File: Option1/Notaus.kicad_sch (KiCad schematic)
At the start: 3 parts, among them Q901 AON6284

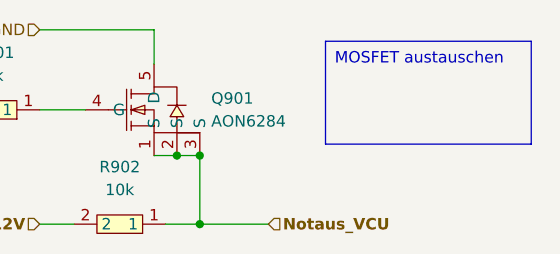
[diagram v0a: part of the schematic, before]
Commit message: SPI Flash hinzugefügt, IN/Outputs vereinheitlicht, USB Flash Möglichkeit hinzugefügt, Display fehtl noch
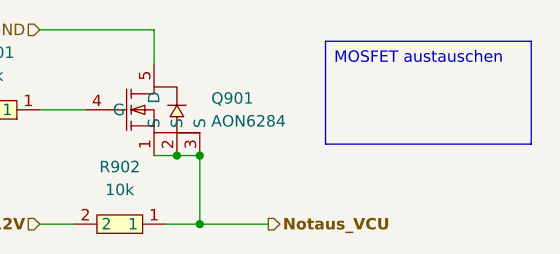
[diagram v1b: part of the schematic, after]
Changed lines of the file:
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@@
 (kicad_sch
-	(version 20231120)
+	(version 20250114)
 	(generator "eeschema")
-	(generator_version "8.0")
+	(generator_version "9.0")
 	(paper "A4")
 	(title_block
@@
 		(comment 2 "Bachelorarbiet")
 		(comment 3 "Sebastian Hampl")
+	)
+	(text_box "MOSFET austauschen"
+		(exclude_from_sim no)
+		(at 132.08 64.77 0)
+		(size 22.86 11.43)
+		(margins 0.9525 0.9525 0.9525 0.9525)
+		(stroke
+			(width 0)
+			(type default)
+			(color 255 0 0 1)
+		)
+		(fill
+			(type none)
+		)
+		(effects
+			(font
+				(size 1.27 1.27)
+			)
+			(justify left top)
+		)
 	)
 	(junction
@@
 		)
 	)
-	(text_box "MOSFET austauschen"
-		(exclude_from_sim no)
-		(at 132.08 64.77 0)
-		(size 22.86 11.43)
-		(stroke
-			(width 0)
-			(type default)
-			(color 255 0 0 1)
-		)
-		(fill
-			(type none)
-		)
-		(effects
-			(font
-				(size 1.27 1.27)
-			)
-			(justify left top)
-		)
-	)
 	(hierarchical_label "Notaus_VCU"
-		(shape input)
+		(shape output)
 		(at 125.73 85.09 0)
 		(effects

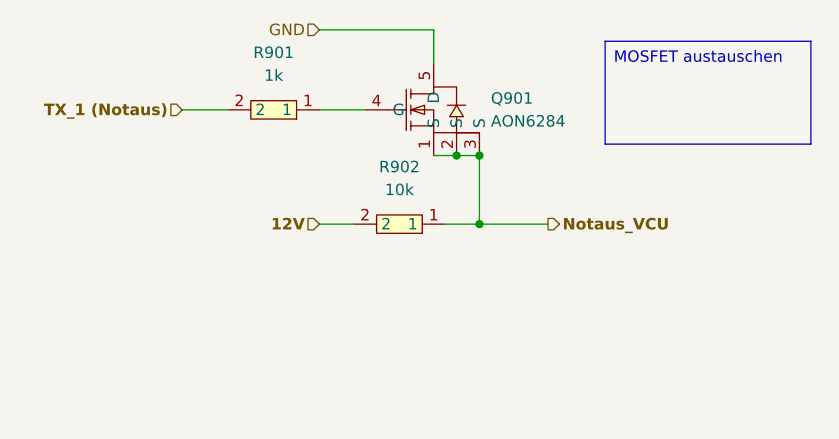
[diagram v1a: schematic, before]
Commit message: USB auf 3V3 umgebaut
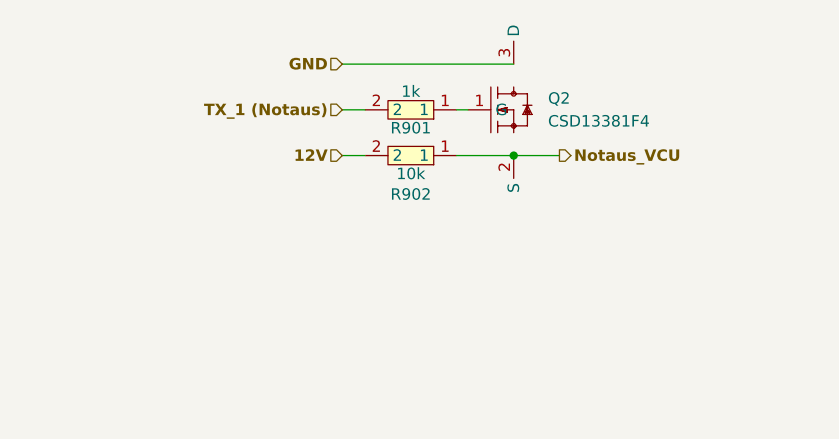
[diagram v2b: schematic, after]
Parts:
- removed Q901: AON6284, easyeda2kicad:POWERVDFN-8_L6.2-W5.2-P1.27-LS6.0-BL, symbol easyeda2kicad:AON6284
- added Q2: CSD13381F4, easyeda2kicad:PICOSTAR-3_L1.0-W0.6-P0.40-S0.65-BL-1, symbol EasyEda2KiCad:CSD13381F4
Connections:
- net GND: now also Q2.3 (D)
- net Notaus_VCU: now also Q2.2 (S)
- net at R901.1: now also Q2.1 (G)
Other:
- moved on the sheet: R901, R902

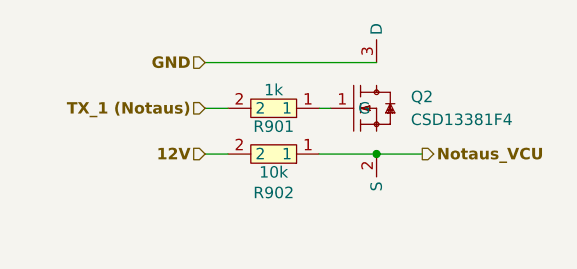
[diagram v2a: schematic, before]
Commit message: Transitor getauscht, Pulldown Widerstände für Definierten LOW Pegel hinzugefügt
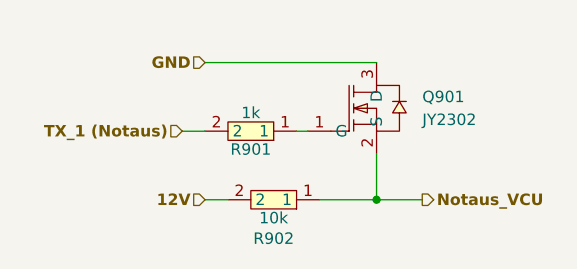
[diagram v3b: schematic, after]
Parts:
- removed Q2: CSD13381F4, easyeda2kicad:PICOSTAR-3_L1.0-W0.6-P0.40-S0.65-BL-1, symbol EasyEda2KiCad:CSD13381F4
- added Q901: JY2302, easyeda2kicad:SOT-23-3_L2.9-W1.3-P0.95-LS2.4-BR, symbol EasyEda2KiCad:JY2302
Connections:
- net GND: now also Q901.3 (D)
- net Notaus_VCU: now also Q901.2 (S)
- net at R901.1: now also Q901.1 (G)
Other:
- moved on the sheet: R901, R902
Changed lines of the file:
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@@
 	)
 	(junction
-		(at 121.92 77.47)
+		(at 121.92 82.55)
 		(diameter 0)
 		(color 0 0 0 0)
@@
 	(wire
 		(pts
-			(xy 121.92 77.47) (xy 127 77.47)
-		)
-		(stroke
-			(width 0)
-			(type default)
-		)
-	)
-	(wire
-		(pts
-			(xy 116.84 72.39) (xy 115.57 72.39)
-		)
-		(stroke
-			(width 0)
-			(type default)
-		)
-	)
-	(wire
-		(pts
-			(xy 102.87 72.39) (xy 105.41 72.39)
-		)
-		(stroke
-			(width 0)
-			(type default)
-		)
-	)
-	(wire
-		(pts
-			(xy 115.57 77.47) (xy 121.92 77.47)
-		)
-		(stroke
-			(width 0)
-			(type default)
-		)
-	)
-	(wire
-		(pts
-			(xy 102.87 77.47) (xy 105.41 77.47)
+			(xy 115.57 82.55) (xy 121.92 82.55)
+		)
+		(stroke
+			(width 0)
+			(type default)
+		)
+	)
+	(wire
+		(pts
+			(xy 114.3 74.93) (xy 113.03 74.93)
+		)
+		(stroke
+			(width 0)
+			(type default)
+		)
+	)
+	(wire
+		(pts
+			(xy 121.92 82.55) (xy 127 82.55)
+		)
+		(stroke
+			(width 0)
+			(type default)
+		)
+	)
+	(wire
+		(pts
+			(xy 100.33 74.93) (xy 102.87 74.93)
+		)
+		(stroke
+			(width 0)
+			(type default)
+		)
+	)
+	(wire
+		(pts
+			(xy 121.92 82.55) (xy 121.92 77.47)
+		)
+		(stroke
+			(width 0)
+			(type default)
+		)
+	)
+	(wire
+		(pts
+			(xy 102.87 82.55) (xy 105.41 82.55)
 		)
 		(stroke
@@
 	(hierarchical_label "Notaus_VCU"
 		(shape output)
-		(at 127 77.47 0)
+		(at 127 82.55 0)
 		(effects
 			(font
@@
 	(hierarchical_label "12V"
 		(shape input)
-		(at 102.87 77.47 180)
+		(at 102.87 82.55 180)
 		(effects
 			(font
@@
 	(hierarchical_label "TX_1 (Notaus)"
 		(shape input)
-		(at 102.87 72.39 180)
+		(at 100.33 74.93 180)
 		(effects
 			(font
@@
 	(symbol
 		(lib_id "easyeda2kicad:0603WAF1001T5E")
-		(at 110.49 72.39 180)
+		(at 107.95 74.93 180)
 		(unit 1)
 		(exclude_from_sim no)
@@
 		(dnp no)
 		(property "Reference" "R901"
-			(at 110.49 74.422 0)
+			(at 107.95 76.962 0)
 			(effects
 				(font
@@
 		)
 		(property "Value" "1k"
-			(at 110.49 70.358 0)
+			(at 107.95 72.898 0)
 			(effects
 				(font
@@
 		)
 		(property "Footprint" "easyeda2kicad:R0603"
-			(at 110.49 64.77 0)
+			(at 107.95 67.31 0)
 			(effects
 				(font
@@
 		)
 		(property "Datasheet" "https://lcsc.com/product-detail/Chip-Resistor-Surface-Mount-UniOhm_1KR-1001-1_C21190.html"
-			(at 110.49 62.23 0)
+			(at 107.95 64.77 0)
 			(effects
 				(font
@@
 		)
 		(property "Description" ""
-			(at 110.49 72.39 0)
+			(at 107.95 74.93 0)
 			(effects
 				(font
@@
 		)
 		(property "LCSC Part" "C21190"
-			(at 110.49 59.69 0)
+			(at 107.95 62.23 0)
 			(effects
 				(font
@@
 	)
 	(symbol
-		(lib_id "EasyEda2KiCad:CSD13381F4")
+		(lib_id "EasyEda2KiCad:JY2302")
 		(at 119.38 72.39 0)
 		(unit 1)
@@
 		(dnp no)
 		(fields_autoplaced yes)
-		(property "Reference" "Q2"
-			(at 125.73 71.1199 0)
+		(property "Reference" "Q901"
+			(at 127 71.1199 0)
 			(effects
 				(font
@@
 			)
 		)
-		(property "Value" "CSD13381F4"
-			(at 125.73 73.6599 0)
+		(property "Value" "JY2302"
+			(at 127 73.6599 0)
 			(effects
 				(font
@@
 			)
 		)
-		(property "Footprint" "easyeda2kicad:PICOSTAR-3_L1.0-W0.6-P0.40-S0.65-BL-1"
+		(property "Footprint" "easyeda2kicad:SOT-23-3_L2.9-W1.3-P0.95-LS2.4-BR"
 			(at 119.38 85.09 0)
 			(effects
@@
 			)
 		)
-		(property "LCSC Part" "C179868"
+		(property "LCSC Part" "C3038095"
 			(at 119.38 87.63 0)
 			(effects
@@
 			)
 		)
+		(pin "2"
+		)
+		(pin "1"
+		)
 		(pin "3"
 		)
-		(pin "1"
-		)
-		(pin "2"
-		)
 		(instances
-			(project "Option1"
+			(project ""
 				(path "/b9e5f262-9648-4b79-bdd1-af888b822329/75c49fff-0cff-45a7-88f1-e27f7e1370db"
-					(reference "Q2")
+					(reference "Q901")
 					(unit 1)
 				)
@@
 	(symbol
 		(lib_id "easyeda2kicad:0603WAF1002T5E")
-		(at 110.49 77.47 180)
+		(at 110.49 82.55 180)
 		(unit 1)
 		(exclude_from_sim no)
@@
 		(dnp no)
 		(property "Reference" "R902"
-			(at 110.49 81.788 0)
+			(at 110.49 86.868 0)
 			(effects
 				(font
@@
 		)
 		(property "Value" "10k"
-			(at 110.49 79.502 0)
+			(at 110.49 84.582 0)
 			(effects
 				(font
@@
 		)
 		(property "Footprint" "easyeda2kicad:R0603"
+			(at 110.49 74.93 0)
+			(effects
+				(font
+					(size 1.27 1.27)
+				)
+				(hide yes)
+			)
+		)
+		(property "Datasheet" "https://lcsc.com/product-detail/Chip-Resistor-Surface-Mount-UniOhm_10KR-1002-1_C25804.html"
+			(at 110.49 72.39 0)
+			(effects
+				(font
+					(size 1.27 1.27)
+				)
+				(hide yes)
+			)
+		)
+		(property "Description" ""
+			(at 110.49 82.55 0)
+			(effects
+				(font
+					(size 1.27 1.27)
+				)
+				(hide yes)
+			)
+		)
+		(property "LCSC Part" "C25804"
 			(at 110.49 69.85 0)
 			(effects
 				(font
-					(size 1.27 1.27)
-				)
-				(hide yes)
-			)
-		)
-		(property "Datasheet" "https://lcsc.com/product-detail/Chip-Resistor-Surface-Mount-UniOhm_10KR-1002-1_C25804.html"
-			(at 110.49 67.31 0)
-			(effects
-				(font
-					(size 1.27 1.27)
-				)
-				(hide yes)
-			)
-		)
-		(property "Description" ""
-			(at 110.49 77.47 0)
-			(effects
-				(font
-					(size 1.27 1.27)
-				)
-				(hide yes)
-			)
-		)
-		(property "LCSC Part" "C25804"
-			(at 110.49 64.77 0)
-			(effects
-				(font

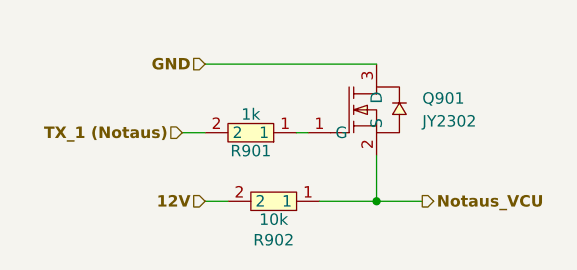
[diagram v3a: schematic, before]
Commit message: MCT und SPI zu Layout hinzugefügt
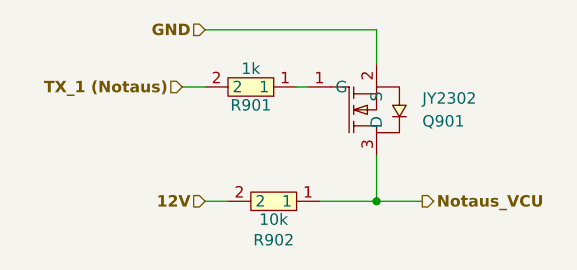
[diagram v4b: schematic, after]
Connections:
- net GND: now also Q901.2 (S); no longer Q901.3 (D)
- net Notaus_VCU: now also Q901.3 (D); no longer Q901.2 (S)
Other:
- moved on the sheet: R901
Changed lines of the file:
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@@
 	(wire
 		(pts
-			(xy 102.87 67.31) (xy 121.92 67.31)
+			(xy 102.87 63.5) (xy 121.92 63.5)
 		)
 		(stroke
@@
 	(wire
 		(pts
-			(xy 114.3 74.93) (xy 113.03 74.93)
+			(xy 100.33 69.85) (xy 102.87 69.85)
+		)
+		(stroke
+			(width 0)
+			(type default)
+		)
+	)
+	(wire
+		(pts
+			(xy 114.3 69.85) (xy 113.03 69.85)
 		)
 		(stroke
@@
 	(wire
 		(pts
-			(xy 100.33 74.93) (xy 102.87 74.93)
+			(xy 121.92 63.5) (xy 121.92 67.31)
 		)
 		(stroke
@@
 	(hierarchical_label "TX_1 (Notaus)"
 		(shape input)
-		(at 100.33 74.93 180)
+		(at 100.33 69.85 180)
 		(effects
 			(font
@@
 	(hierarchical_label "GND"
 		(shape input)
-		(at 102.87 67.31 180)
+		(at 102.87 63.5 180)
 		(effects
 			(font
@@
 	(symbol
 		(lib_id "easyeda2kicad:0603WAF1001T5E")
-		(at 107.95 74.93 180)
+		(at 107.95 69.85 180)
 		(unit 1)
 		(exclude_from_sim no)
@@
 		(dnp no)
 		(property "Reference" "R901"
-			(at 107.95 76.962 0)
+			(at 107.95 71.882 0)
 			(effects
 				(font
@@
 		)
 		(property "Value" "1k"
-			(at 107.95 72.898 0)
+			(at 107.95 67.818 0)
 			(effects
 				(font
@@
 		)
 		(property "Footprint" "easyeda2kicad:R0603"
-			(at 107.95 67.31 0)
+			(at 107.95 62.23 0)
 			(effects
 				(font
@@
 		)
 		(property "Datasheet" "https://lcsc.com/product-detail/Chip-Resistor-Surface-Mount-UniOhm_1KR-1001-1_C21190.html"
-			(at 107.95 64.77 0)
+			(at 107.95 59.69 0)
 			(effects
 				(font
@@
 		)
 		(property "Description" ""
-			(at 107.95 74.93 0)
+			(at 107.95 69.85 0)
 			(effects
 				(font
@@
 		)
 		(property "LCSC Part" "C21190"
-			(at 107.95 62.23 0)
+			(at 107.95 57.15 0)
 			(effects
 				(font
@@
 		(lib_id "EasyEda2KiCad:JY2302")
 		(at 119.38 72.39 0)
+		(mirror x)
 		(unit 1)
 		(exclude_from_sim no)
@@
 		(on_board yes)
 		(dnp no)
-		(fields_autoplaced yes)
 		(property "Reference" "Q901"
-			(at 127 71.1199 0)
+			(at 127 73.6601 0)
 			(effects
 				(font
@@
 		)
 		(property "Value" "JY2302"
-			(at 127 73.6599 0)
+			(at 127 71.1201 0)
 			(effects
 				(font
@@
 		)
 		(property "Footprint" "easyeda2kicad:SOT-23-3_L2.9-W1.3-P0.95-LS2.4-BR"
-			(at 119.38 85.09 0)
+			(at 119.38 59.69 0)
 			(effects
 				(font
@@
 		)
 		(property "LCSC Part" "C3038095"
-			(at 119.38 87.63 0)
-			(effects
-				(font
+			(at 119.38 57.15 0)
+			(effects
+				(font

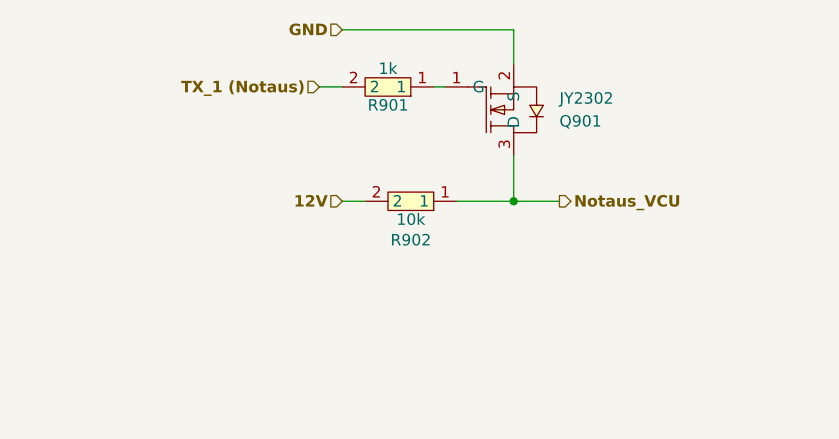
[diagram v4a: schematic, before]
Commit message: LEDs an Transistoren hinzugefügt, Layout angepasst, LEDs eingefügt, LEDs zeigen an, ob Transsitor durchgeschalten ist
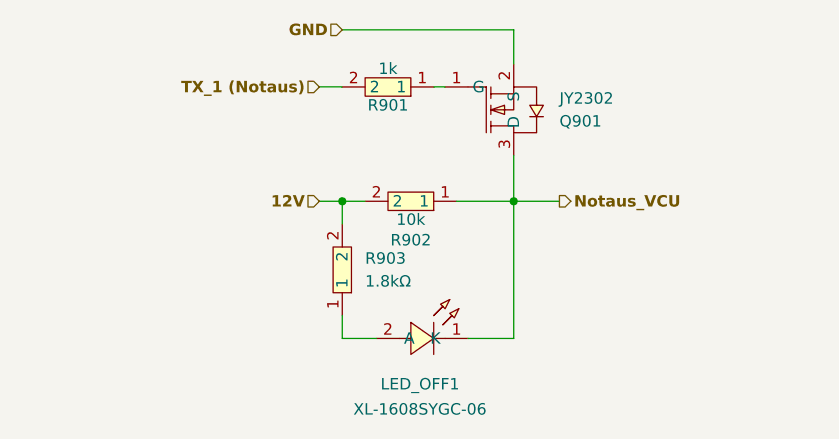
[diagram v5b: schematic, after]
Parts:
- added LED_OFF1: XL-1608SYGC-06, easyeda2kicad:LED0603-RD_GREEN, symbol EasyEda2KiCad:XL-1608SYGC-06
- added R903: 1.8kΩ, easyeda2kicad:R0603, symbol EasyEda2KiCad:0603WAF1801T5E
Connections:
- net 12V: now also R903.2
- net Notaus_VCU: now also LED_OFF1.1 (K)
- new net: LED_OFF1.2 (A), R903.1
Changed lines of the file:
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@@
 		(color 0 0 0 0)
 	)
+	(junction
+		(at 102.87 82.55)
+		(diameter 0)
+		(color 0 0 0 0)
+	)
+	(wire
+		(pts
+			(xy 102.87 82.55) (xy 102.87 85.09)
+		)
+		(stroke
+			(width 0)
+			(type default)
+		)
+	)
+	(wire
+		(pts
+			(xy 102.87 82.55) (xy 105.41 82.55)
+		)
+		(stroke
+			(width 0)
+			(type default)
+		)
+	)
+	(wire
+		(pts
+			(xy 116.84 97.79) (xy 121.92 97.79)
+		)
+		(stroke
+			(width 0)
+			(type default)
+		)
+	)
 	(wire
 		(pts
@@
 	(wire
 		(pts
+			(xy 106.68 97.79) (xy 102.87 97.79)
+		)
+		(stroke
+			(width 0)
+			(type default)
+		)
+	)
+	(wire
+		(pts
+			(xy 121.92 97.79) (xy 121.92 82.55)
+		)
+		(stroke
+			(width 0)
+			(type default)
+		)
+	)
+	(wire
+		(pts
 			(xy 121.92 63.5) (xy 121.92 67.31)
 		)
@@
 	(wire
 		(pts
+			(xy 102.87 97.79) (xy 102.87 95.25)
+		)
+		(stroke
+			(width 0)
+			(type default)
+		)
+	)
+	(wire
+		(pts
 			(xy 121.92 82.55) (xy 121.92 77.47)
 		)
@@
 	(wire
 		(pts
-			(xy 102.87 82.55) (xy 105.41 82.55)
+			(xy 100.33 82.55) (xy 102.87 82.55)
 		)
 		(stroke
@@
 	(hierarchical_label "12V"
 		(shape input)
-		(at 102.87 82.55 180)
+		(at 100.33 82.55 180)
 		(effects
 			(font
@@
 					(unit 1)
 				)
+			)
+		)
+	)
+	(symbol
+		(lib_id "EasyEda2KiCad:XL-1608SYGC-06")
+		(at 111.76 97.79 0)
+		(mirror y)
+		(unit 1)
+		(exclude_from_sim no)
+		(in_bom yes)
+		(on_board yes)
+		(dnp no)
+		(property "Reference" "LED_OFF1"
+			(at 111.506 102.87 0)
+			(effects
+				(font
+					(size 1.27 1.27)
+				)
+			)
+		)
+		(property "Value" "XL-1608SYGC-06"
+			(at 111.506 105.664 0)
+			(effects
+				(font
+					(size 1.27 1.27)
+				)
+			)
+		)
+		(property "Footprint" "easyeda2kicad:LED0603-RD_GREEN"
+			(at 111.76 105.41 0)
+			(effects
+				(font
+					(size 1.27 1.27)
+				)
+				(hide yes)
+			)
+		)
+		(property "Datasheet" ""
+			(at 111.76 97.79 0)
+			(effects
+				(font
+					(size 1.27 1.27)
+				)
+				(hide yes)
+			)
+		)
+		(property "Description" ""
+			(at 111.76 97.79 0)
+			(effects
+				(font
+					(size 1.27 1.27)
+				)
+				(hide yes)
+			)
+		)
+		(property "LCSC Part" "C965805"
+			(at 111.76 107.95 0)
+			(effects
+				(font
+					(size 1.27 1.27)
+				)
+				(hide yes)
+			)
+		)
+		(pin "2"
+		)
+		(pin "1"
+		)
+		(instances
+			(project "Option1"
+				(path "/b9e5f262-9648-4b79-bdd1-af888b822329/75c49fff-0cff-45a7-88f1-e27f7e1370db"
+					(reference "LED_OFF1")
+					(unit 1)
+				)
+			)
+		)
+	)
+	(symbol
+		(lib_id "EasyEda2KiCad:0603WAF1801T5E")
+		(at 102.87 90.17 270)
+		(mirror x)
+		(unit 1)
+		(exclude_from_sim no)
+		(in_bom yes)
+		(on_board yes)
+		(dnp no)
+		(fields_autoplaced yes)
+		(property "Reference" "R903"
+			(at 105.41 88.8999 90)
+			(effects
+				(font
+					(size 1.27 1.27)
+				)
+				(justify left)
+			)
+		)
+		(property "Value" "1.8kΩ"
+			(at 105.41 91.4399 90)
+			(effects
+				(font
+					(size 1.27 1.27)
+				)
+				(justify left)
+			)
+		)
+		(property "Footprint" "easyeda2kicad:R0603"
+			(at 95.25 90.17 0)
+			(effects
+				(font
+					(size 1.27 1.27)
+				)
+				(hide yes)
+			)
+		)
+		(property "Datasheet" "https://lcsc.com/product-detail/Chip-Resistor-Surface-Mount-UniOhm_1-8KR-1801-1_C4177.html"
+			(at 92.71 90.17 0)
+			(effects
+				(font
+					(size 1.27 1.27)
+				)
+				(hide yes)
+			)
+		)
+		(property "Description" ""
+			(at 102.87 90.17 0)
+			(effects
+				(font
+					(size 1.27 1.27)
+				)
+				(hide yes)
+			)
+		)
+		(property "LCSC Part" "C4177"
+			(at 90.17 90.17 0)
+			(effects
+				(font
+					(size 1.27 1.27)
+				)
+				(hide yes)
+			)
+		)
+		(pin "1"
+		)
+		(pin "2"
+		)
+		(instances
+			(project "Option1"
+				(path "/b9e5f262-9648-4b79-bdd1-af888b822329/75c49fff-0cff-45a7-88f1-e27f7e1370db"
+					(reference "R903")
+					(unit 1)
+				)
